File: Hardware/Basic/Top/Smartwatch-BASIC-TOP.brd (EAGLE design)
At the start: 38 x 38 mm, 59 parts, among them SW6 SWITCH.MOM, SW7 SWITCH.MOM, U2 NRF52832_MODULE_MDBT42, U4 FT231XS

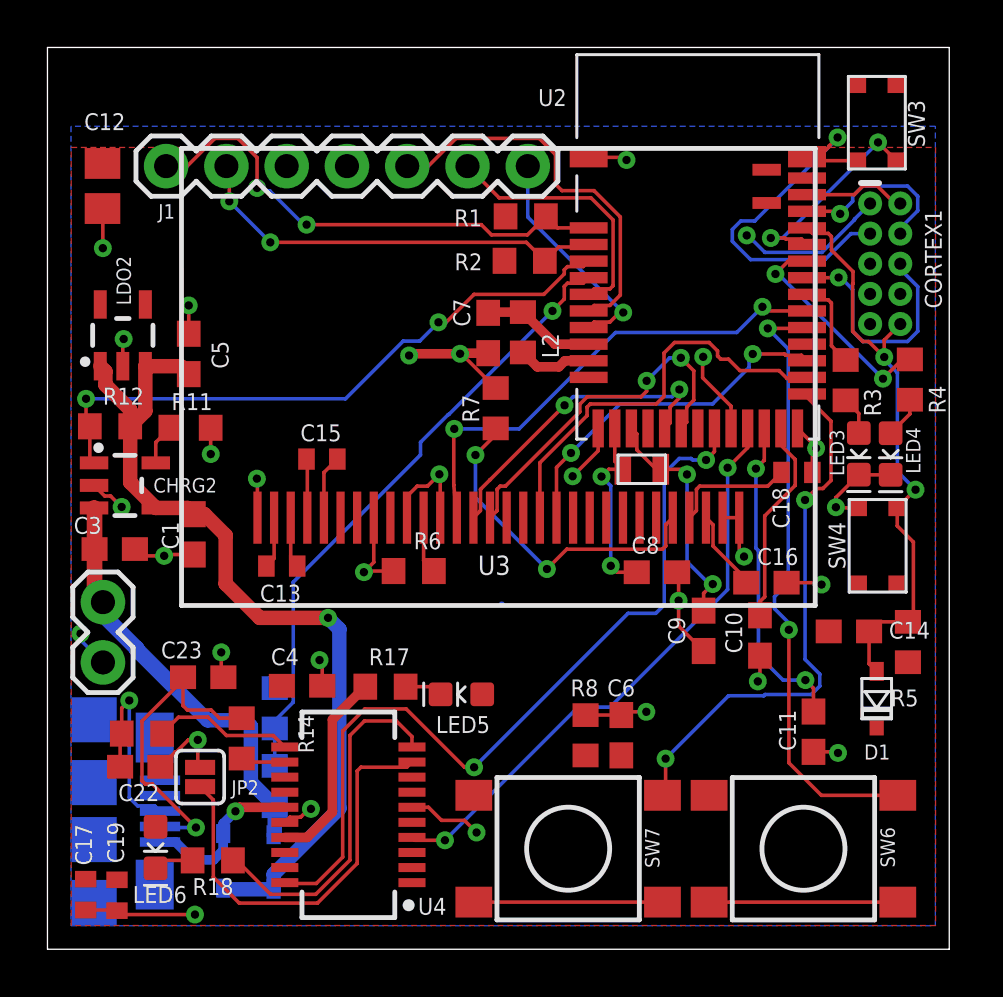
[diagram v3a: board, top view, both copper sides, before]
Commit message: Header Pins Fixed
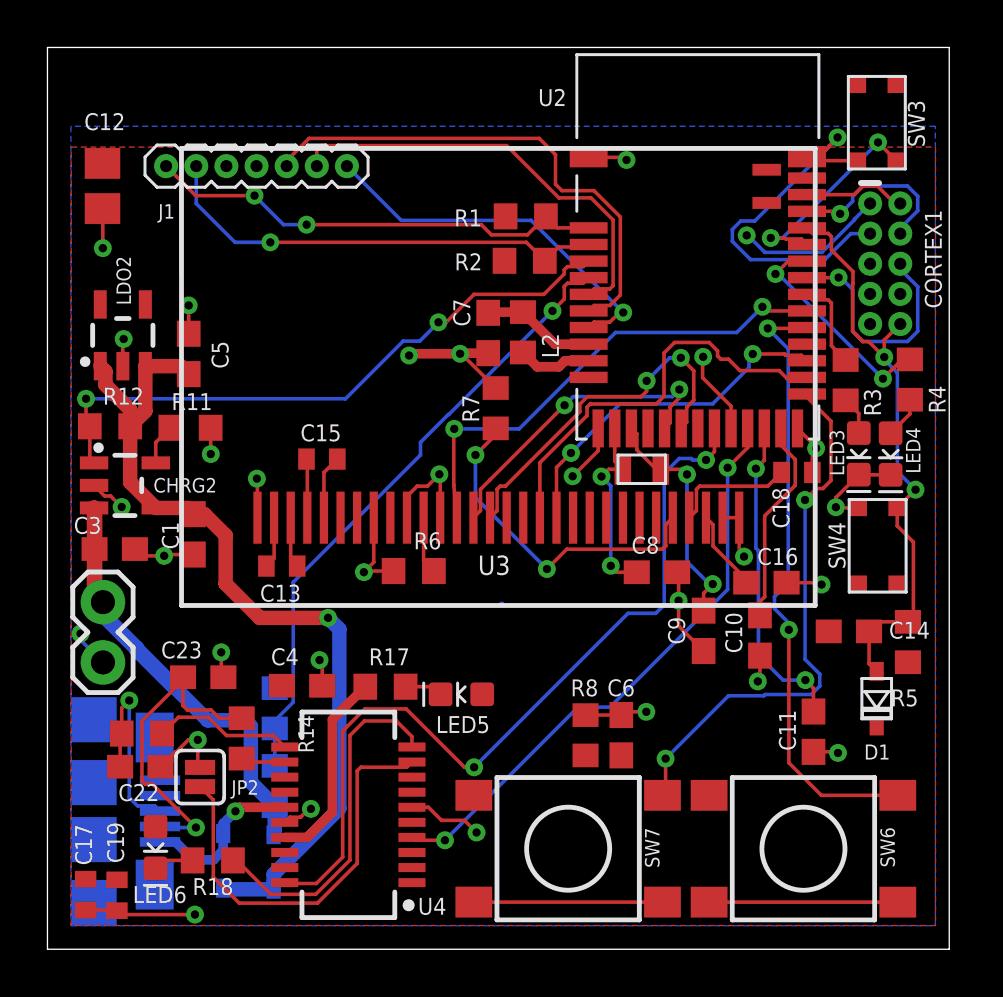
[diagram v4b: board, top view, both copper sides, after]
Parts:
- J1: device LinnesLab-Connectors:1X07 -> LinnesLab-Connectors:1X07_1.27MM
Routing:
- net D29/LED.CTRL: track 11.0 -> 18.5 mm
- net A7/PPG: track 9.55 -> 15.9 mm
- net A6/TIA: track 16.5 -> 21.7 mm
- net SDA: track 21.2 -> 19.7 mm
- net SCL: track 18.0 -> 19.4 mm, vias 2 -> 1
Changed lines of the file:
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@@
 <attribute name="VALUE" x="21.9404" y="7.411921875" size="0.6096" layer="27" ratio="20" rot="R180" align="top-center"/>
 </element>
-<element name="J1" library="LinnesLab-Connectors" package="1X07" value="" x="5" y="33" smashed="yes">
+<element name="J1" library="LinnesLab-Connectors" package="1X07_1.27MM" value="" x="5" y="33" smashed="yes">
 <attribute name="NAME" x="4.6698" y="30.7876625" size="0.6096" layer="25" font="vector" ratio="20"/>
 <attribute name="VALUE" x="3.73" y="30.968" size="0.6096" layer="27" font="vector" ratio="20"/>
@@
 <contactref element="R2" pad="2"/>
 <polygon width="0.1524" layer="1">
-<vertex x="1" y="33.786896875"/>
-<vertex x="37.421640625" y="33.786896875"/>
+<vertex x="1" y="33.8021375"/>
+<vertex x="37.421640625" y="33.8021375"/>
 <vertex x="37.421640625" y="1"/>
 <vertex x="1" y="1"/>
@@
 <contactref element="C6" pad="1"/>
 <contactref element="R8" pad="2"/>
+<wire x1="2.31901875" y1="33.11148125" x2="8.81" y2="33" width="0" layer="19" extent="1-1"/>
 </signal>
 <signal name="P0.09/NFC1">
@@
 <contactref element="R1" pad="1"/>
 <contactref element="J1" pad="1"/>
-<wire x1="7.05603125" y1="34.1684" x2="8.02396875" y2="34.1684" width="0.1524" layer="1"/>
-<wire x1="8.02396875" y1="34.1684" x2="8.832859375" y2="33.359509375" width="0.1524" layer="1"/>
-<wire x1="5" y1="33" x2="5.88763125" y2="33" width="0.1524" layer="1"/>
-<wire x1="5.88763125" y1="33" x2="7.05603125" y2="34.1684" width="0.1524" layer="1"/>
-<wire x1="8.832859375" y1="33.359509375" x2="8.832859375" y2="32.07891875" width="0.1524" layer="1"/>
 <wire x1="10.91971875" y1="30.533078125" x2="10.79525625" y2="30.533078125" width="0.1524" layer="16"/>
-<wire x1="10.79525625" y1="30.533078125" x2="9.373878125" y2="31.95445625" width="0.1524" layer="16"/>
-<wire x1="9.373878125" y1="31.95445625" x2="8.957321875" y2="31.95445625" width="0.1524" layer="16"/>
-<wire x1="8.832859375" y1="32.07891875" x2="8.957321875" y2="31.95445625" width="0.1524" layer="16"/>
 <wire x1="18.281240625" y1="30.533078125" x2="18.70975625" y2="30.1045625" width="0.1524" layer="1"/>
 <wire x1="18.70975625" y1="30.1045625" x2="20.22584375" y2="30.1045625" width="0.1524" layer="1"/>
@@
 <wire x1="21.004440625" y1="30.883159375" x2="21.4906" y2="30.397" width="0.1524" layer="1"/>
 <wire x1="21.4906" y1="30.397" x2="22.806" y2="30.397" width="0.1524" layer="1"/>
-<via x="8.832859375" y="32.07891875" extent="1-16" drill="0.35"/>
 <via x="10.91971875" y="30.533078125" extent="1-16" drill="0.35"/>
+<via x="8.7249" y="31.75508125" extent="1-16" drill="0.35"/>
+<wire x1="8.7249" y1="31.75508125" x2="6.24491875" y2="31.75508125" width="0.1524" layer="1"/>
+<wire x1="6.24491875" y1="31.75508125" x2="5" y2="33" width="0.1524" layer="1"/>
+<wire x1="8.7249" y1="31.75508125" x2="9.946903125" y2="30.533078125" width="0.1524" layer="16"/>
+<wire x1="9.946903125" y1="30.533078125" x2="10.91971875" y2="30.533078125" width="0.1524" layer="16"/>
 </signal>
 <signal name="SCL">
@@
 <contactref element="J1" pad="2"/>
 <wire x1="22.806" y1="29.697" x2="22.7016" y2="29.5926" width="0.1524" layer="1"/>
-<wire x1="9.389796875" y1="29.7887625" x2="7.66191875" y2="31.516640625" width="0.1524" layer="16"/>
-<wire x1="7.54" y1="33" x2="7.66191875" y2="32.87808125" width="0.1524" layer="1"/>
-<wire x1="7.66191875" y1="32.87808125" x2="7.66191875" y2="31.516640625" width="0.1524" layer="1"/>
+<wire x1="9.389796875" y1="29.7887625" x2="7.90389375" y2="29.7887625" width="0.1524" layer="16"/>
 <wire x1="20.180121875" y1="29.7887625" x2="20.958721875" y2="29.0101625" width="0.1524" layer="1"/>
 <wire x1="9.389796875" y1="29.7887625" x2="20.180121875" y2="29.7887625" width="0.1524" layer="1"/>
@@
 <wire x1="22.7016" y1="29.5926" x2="21.541159375" y2="29.5926" width="0.1524" layer="1"/>
 <via x="9.389796875" y="29.7887625" extent="1-16" drill="0.35"/>
-<via x="7.66191875" y="31.516640625" extent="1-16" drill="0.35"/>
+<wire x1="6.27" y1="31.42265625" x2="6.27" y2="33" width="0.1524" layer="16"/>
+<wire x1="7.90389375" y1="29.7887625" x2="6.27" y2="31.42265625" width="0.1524" layer="16"/>
 </signal>
 <signal name="SCK">
@@
 <contactref element="J1" pad="6"/>
 <wire x1="23.7006875" y1="27.8284" x2="23.8346" y2="27.9623125" width="0.1524" layer="1"/>
-<wire x1="19.03824375" y1="31.66175625" x2="17.7" y2="33" width="0.1524" layer="1"/>
 <wire x1="22.806" y1="27.597" x2="23.0374" y2="27.8284" width="0.1524" layer="1"/>
 <wire x1="23.0374" y1="27.8284" x2="23.7006875" y2="27.8284" width="0.1524" layer="1"/>
 <wire x1="23.8346" y1="27.9623125" x2="23.8346" y2="30.7316875" width="0.1524" layer="1"/>
 <wire x1="23.8346" y1="30.7316875" x2="22.90453125" y2="31.66175625" width="0.1524" layer="1"/>
-<wire x1="22.90453125" y1="31.66175625" x2="19.03824375" y2="31.66175625" width="0.1524" layer="1"/>
+<wire x1="22.90453125" y1="31.66175625" x2="21.55391875" y2="31.66175625" width="0.1524" layer="1"/>
+<wire x1="19.352075" y1="33.8636" x2="11.534140625" y2="33.8636" width="0.1524" layer="1"/>
+<wire x1="21.55391875" y1="31.66175625" x2="19.352075" y2="33.8636" width="0.1524" layer="1"/>
+<wire x1="11.534140625" y1="33.8636" x2="11.35" y2="33.679459375" width="0.1524" layer="1"/>
+<wire x1="11.35" y1="33.679459375" x2="11.35" y2="33" width="0.1524" layer="1"/>
 </signal>
 <signal name="A6/TIA">
@@
 <wire x1="21.680178125" y1="31.96655625" x2="21.4084" y2="32.238334375" width="0.1524" layer="1"/>
 <wire x1="21.4084" y1="32.238334375" x2="21.4084" y2="33.48396875" width="0.1524" layer="1"/>
-<wire x1="16.04763125" y1="33" x2="15.16" y2="33" width="0.1524" layer="1"/>
-<wire x1="17.21603125" y1="34.1684" x2="16.04763125" y2="33" width="0.1524" layer="1"/>
 <wire x1="23.7006875" y1="27.1284" x2="24.1394" y2="27.5671125" width="0.1524" layer="1"/>
 <wire x1="24.1394" y1="27.5671125" x2="24.1394" y2="30.85794375" width="0.1524" layer="1"/>
-<wire x1="20.72396875" y1="34.1684" x2="17.21603125" y2="34.1684" width="0.1524" layer="1"/>
+<wire x1="20.72396875" y1="34.1684" x2="11.0235125" y2="34.1684" width="0.1524" layer="1"/>
+<wire x1="11.0235125" y1="34.1684" x2="10.08" y2="33.2248875" width="0.1524" layer="1"/>
+<wire x1="10.08" y1="33.2248875" x2="10.08" y2="33" width="0.1524" layer="1"/>
 </signal>
 <signal name="A7/PPG">
@@
 <wire x1="24.1032875" y1="26.831" x2="24.2614375" y2="26.831" width="0.1524" layer="1"/>
 <wire x1="23.7006875" y1="26.4284" x2="24.1032875" y2="26.831" width="0.1524" layer="1"/>
-<wire x1="24.2614375" y1="26.831" x2="20.24" y2="30.8524375" width="0.1524" layer="16"/>
-<wire x1="20.24" y1="30.8524375" x2="20.24" y2="33" width="0.1524" layer="16"/>
+<wire x1="24.2614375" y1="26.831" x2="20.37875625" y2="30.71368125" width="0.1524" layer="16"/>
+<wire x1="14.90631875" y1="30.71368125" x2="12.62" y2="33" width="0.1524" layer="16"/>
+<wire x1="20.37875625" y1="30.71368125" x2="14.90631875" y2="30.71368125" width="0.1524" layer="16"/>
 </signal>
 <signal name="N$16">

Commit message: Top Board airwire fixed
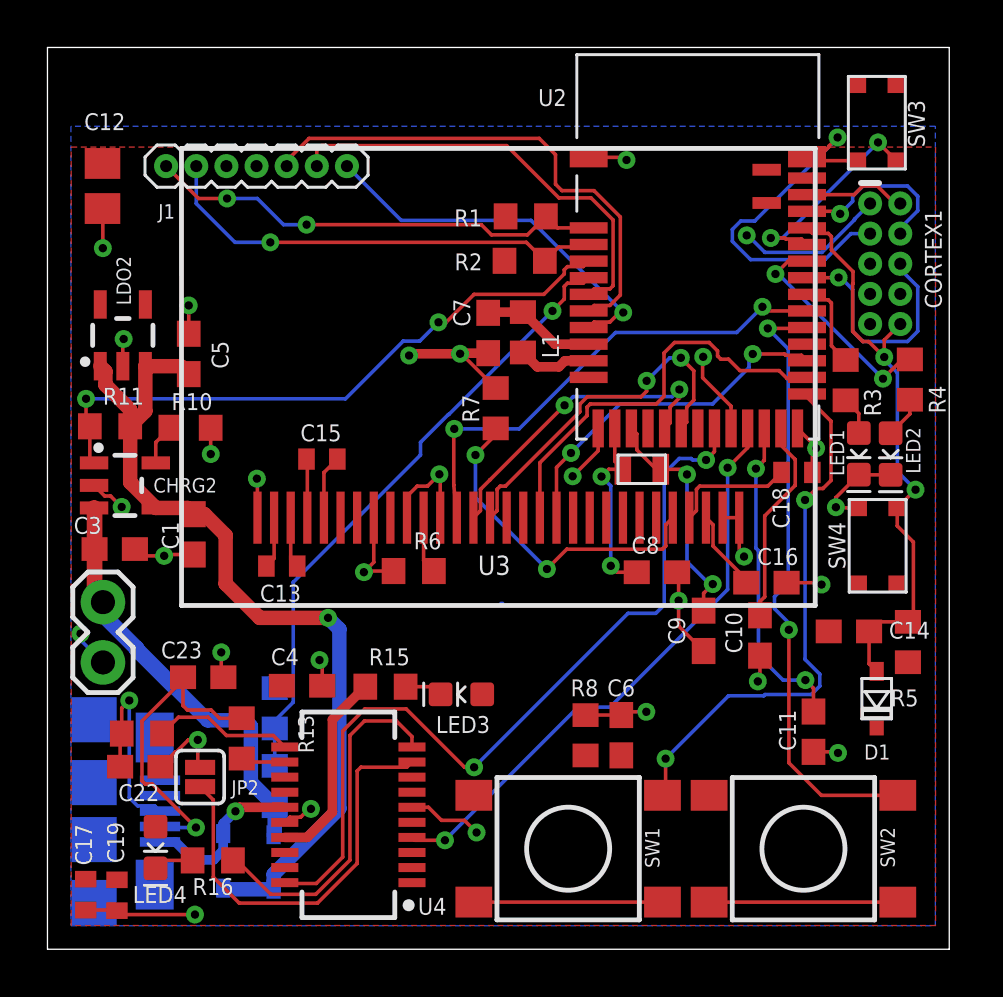
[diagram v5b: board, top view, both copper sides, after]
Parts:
- removed LED5: RED, LinnesLab-LED:LED-0603
- removed LED6: YELLOW, LinnesLab-LED:LED-0603
- removed R18: 1k, LinnesLab-Passives:R0603
- added LED1: RED, LinnesLab-LED:LED-0603
- added LED2: BLUE, LinnesLab-LED:LED-0603
- added R9: 27, LinnesLab-Passives:R0603
- LED4: value BLUE -> YELLOW
- R10: value 27 -> 4.7k
- R11: value (none) -> 100k
- R14: value 100k -> 27
- R16: value 27 -> 1k
- moved LED4 35.1 mm to (4.55, 4.29)
- moved LED3 19.6 mm to (17.4, 10.7), turned to 180 degrees
- moved R12 16.7 mm to (9.58, 6.88), flipped to the bottom, turned to 270 degrees
- moved R10 13.3 mm to (6.03, 22.0), turned to 180 degrees
- moved R16 6.12 mm to (6.97, 3.74), turned to 180 degrees
- moved R14 5.70 mm to (3.98, 9.09), flipped to the top, turned to 0 degrees
- moved R11 3.39 mm to (2.64, 22.0), turned to 0 degrees
- moved R13 3.28 mm to (9.58, 10.2)
- renumbered D4 to D2, D5 to D3, L2 to L1, R17 to R15, SW6 to SW2, SW7 to SW1
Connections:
- net 3.3V: now also LED3.A, LED4.A; no longer LED5.A, LED6.A
- net A4/BATT: now also R12.1, R13.2; no longer R13.1, R14.2
- net D27/CHRG.STAT: now also R11.1; no longer R12.1
- net GND: now also LED1.C, LED2.C, R10.1, R13.1; no longer LED3.C, LED4.C, R11.1, R14.1
- net N$10: now also LED2.A; no longer LED4.A
- net N$16: now also R10.2; no longer R11.2
- net N$25: now also R9.2; no longer R10.2
- net N$26: now also R14.2; no longer R16.2
- net N$27: now also LED3.C; no longer LED5.C
- net N$28: now also LED4.C, R16.2; no longer LED6.C, R18.2
- net N$9: now also LED1.A; no longer LED3.A
- net TXLED: now also R16.1; no longer R18.1
- net USB+: now also R14.1; no longer R16.1
- net USB-: now also R9.1; no longer R10.1
- net VIN: now also R11.2; no longer R12.2
- net VLIPO: now also R12.2; no longer R13.2

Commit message: Top Board BOM WIP
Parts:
- removed C22, C23: 47p, LinnesLab-Passives:C0603
- removed U4: FT231XS, LinnesLab-DigitalIC:SSOP20_L
- added C2: 10u, LinnesLab-Passives:C0805
- added C20: 4.7u, LinnesLab-Passives:C0603
- added U1: NRF52832_MODULE_MDBT42, LinnesLab-Microcontrollers:BLE_MODULE_RAYTAC_MDBT42
- C1: value 4.7u -> 1u
- C10, C11: value 300p -> 2.2uF; device LinnesLab-Passives:C0603 -> LinnesLab-Passives:C0402
- C12: value 10u -> 2.2uF; device LinnesLab-Passives:C0805 -> LinnesLab-Passives:C0402
- C13, C18: value 2.2uF -> 100n; device LinnesLab-Passives:C0402 -> LinnesLab-Passives:C0603
- C14: value 100n -> 4.7u
- C15, C17: value 2.2uF -> 47p; device LinnesLab-Passives:C0402 -> LinnesLab-Passives:C0603
- C16: value 10uF -> 1u
- C19: value 2.2uF -> 1u; device LinnesLab-Passives:C0402 -> LinnesLab-Passives:C0603
- C3: value 4.7u -> (none)
- C4: value 100n -> (none)
- C5, C6: value 1u -> 300p
- C7: value 1u -> 10uF
- C8, C9: value (none) -> 2.2uF; device LinnesLab-Passives:C0603 -> LinnesLab-Passives:C0402
- R10: value 4.7k -> 27
- R11: value 100k -> 4.7k
- R14: value 27 -> 100k
- R6: value 10k -> 390k
- R7: value 390k -> 10k
- SW1: value SWITCH.MOM -> (none); device LinnesLab-Switches:TACTILE_SWITCH_SMD_6.2MM_TALL -> LinnesLab-Switches:BUTTON-GULLWING
- SW3: value (none) -> SWITCH.MOM; device LinnesLab-Switches:BUTTON-GULLWING -> LinnesLab-Switches:TACTILE_SWITCH_SMD_6.2MM_TALL
- U2: value NRF52832_MODULE_MDBT42 -> (none); device LinnesLab-Microcontrollers:BLE_MODULE_RAYTAC_MDBT42 -> LinnesLab-Displays:UG-2864HSWEG01_0.96IN_NO-WRAPAROUND
- U3: value (none) -> FT231XS; device LinnesLab-Displays:UG-2864HSWEG01_0.96IN_NO-WRAPAROUND -> LinnesLab-DigitalIC:SSOP20_L
- moved SW1 33.2 mm to (34.9, 34.8), turned to 90 degrees
- moved C5 30.8 mm to (32.3, 9.17)
- moved SW3 30.7 mm to (31.9, 4.24), turned to 180 degrees
- moved C11 30.1 mm to (2.93, 2.28), turned to 90 degrees
- moved C12 29.9 mm to (1.61, 2.30)
- moved C14 27.9 mm to (6.17, 17.5), turned to 90 degrees
- moved C16 26.2 mm to (5.95, 25.1), turned to 270 degrees
- moved C13 24.1 mm to (33.8, 13.4), turned to 0 degrees
- moved R8 23.9 mm to (2.64, 22.0), turned to 0 degrees
- moved C3 22.9 mm to (25.7, 15.9), turned to 180 degrees
- moved C18 22.7 mm to (10.7, 11.1)
- moved C19 22.3 mm to (24.2, 9.02)
- moved R5 21.0 mm to (15.4, 15.9), turned to 0 degrees
- moved C10 20.4 mm to (9.87, 16.1), turned to 180 degrees
- moved R7 20.0 mm to (36.3, 12.9), turned to 270 degrees
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- renumbered CHRG2 to CHRG1, CORTEX1 to DEBUG1, JP2 to JP1, LDO2 to LDO1, USB2 to USB1, XTAL2 to XTAL1
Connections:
- removed net N$21 (its old number): SW1.B1, SW1.B2
- new net N$22: SW3.B1, SW3.B2
- net !CTS: now also U3.9; no longer U4.9
- net !DTR: now also U3.1; no longer U4.1
- net 3.3V: now also C11.2, C18.2, C19.1, C2.2, R12.2, R7.2, U1.11, U2.6, U2.9, U3.14, U3.3; no longer C17.2, C19.2, C4.2, C6.1, R5.2, R8.2, U2.11, U3.6, U3.9, U4.14, U4.3
- net A4/BATT: now also R13.1, R14.2, U1.5; no longer R12.1, R13.2, U2.5
- net A6/TIA: now also U1.7; no longer U2.7
- net A7/PPG: now also U1.8; no longer U2.8
- net D11/SW1: now also SW2.A1, U1.25; no longer SW1.A1, U2.25
- net D15/SW2: now also SW3.A1, U1.29; no longer SW2.A1, U2.29
- net D16/CS.OLED: now also U1.30, U2.13; no longer U2.30, U3.13
- net D27/CHRG.STAT: now also R8.1, U1.4; no longer R11.1, U2.4
- net D29/LED.CTRL: now also U1.6; no longer U2.6
- net D3/RESET.OLED: now also U1.16, U2.14; no longer U2.16, U3.14
- net D4/DC.OLED: now also U1.17, U2.15; no longer U2.17, U3.15
- net D5/CD1: now also U1.18; no longer U2.18
- net D7/SD.CS: now also U1.20; no longer U2.20
- net DFU: now also SW1.3, U1.34; no longer SW3.3, U2.34
- net DTR: now also C13.1; no longer C14.1
- net FRST: now also U1.38; no longer U2.38
- net FT3V3: now also U3.13; no longer U4.13
- net GND: now also C1.2, C11.1, C14.1, C15.1, C17.2, C19.2, C2.1, C20.2, C3.1, C4.2, C5.2, C7.1, C9.1, R11.1, R12.1, R14.1, R5.1, R6.2, SW1.1, U1.1, U1.12, U1.24, U1.39, U2.10, U2.29, U2.30, U2.8, U3.16, U3.6; no longer C1.1, C10.2, C11.2, C17.1, C19.1, C22.2, C23.1, C3.2, C4.1, C5.1, C7.2, C8.1, C9.2, R10.1, R13.1, R6.1, R7.2, R8.1, SW3.1, U2.24, U2.39, U3.1, U3.10, U3.12, U3.29, U3.30, U3.8, U4.16, U4.6
- net LED1: now also U1.31; no longer U2.31
- net LED2: now also U1.33; no longer U2.33
- net MISO: now also U1.28; no longer U2.28
- net MOSI: now also U1.27, U2.19; no longer U2.27, U3.19
- net N$1: now also R5.2, U2.11; no longer R6.2, U3.11
- net N$11: now also U1.10; no longer U2.10
- net N$12: now also C1.1, U1.9; no longer C7.1, U2.9
- net N$13: now also C7.2, U2.28; no longer C16.2, U3.28
- net N$15: now also C9.2, U2.27; no longer C18.2, U3.27
- net N$16: now also R11.2; no longer R10.2
- net N$2: now also R6.1, U2.26; no longer R7.1, U3.26
- net N$25: now also U3.12; no longer U4.12
- net N$26: now also R10.2, U3.11; no longer R14.2, U4.11
- net N$3: now also C10.2, U2.2; no longer C13.2, U3.2
- net N$4: now also C3.2, U1.13; no longer C8.2, U2.13
- net N$5: now also C10.1, U2.3; no longer C13.1, U3.3
- net N$6: now also C4.1, U1.14; no longer C9.1, U2.14
- net N$7: now also C8.2, U2.4; no longer C15.2, U3.4
- net N$8: now also C8.1, U2.5; no longer C15.1, U3.5
- net P0.09/NFC1: now also C5.1, U1.22; no longer C11.1, U2.22
- net P0.10/NFC2: now also C6.1, U1.23; no longer C10.1, U2.23
- net RESET: now also C13.2, R7.1, U1.35; no longer C14.2, R5.1, U2.35
- net RXD: now also U1.21, U3.4; no longer U2.21, U4.4
- net RXLED: now also U3.17; no longer U4.17
- net SCK: now also U1.26, U2.18; no longer U2.26, U3.18
- net SCL: now also U1.3; no longer U2.3
- net SDA: now also U1.2; no longer U2.2
- net SWCLK: now also U1.36; no longer U2.36
- net SWDIO: now also U1.37; no longer U2.37
- net SWO: now also U1.32; no longer U2.32
- net TXD: now also U1.19, U3.20; no longer U2.19, U4.20
- net TXLED: now also U3.10; no longer U4.10
- net USB+: now also C17.1, R10.1; no longer C22.1, R14.1
- net USB-: now also C15.2; no longer C23.2
- net VIN: now also C14.2, C16.2, R8.2; no longer C1.2, C5.2, R11.2
- net VLIPO: now also C20.1, R13.2; no longer C3.1, R12.2
- net V_USB: now also U3.15; no longer U4.15
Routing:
- net N$22: track 0.00 -> 7.95 mm
- net N$21 (its old number): track 7.95 -> 0.00 mm
